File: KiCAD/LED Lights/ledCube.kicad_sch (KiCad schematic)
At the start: 14 parts, among them P1 CONN_01X03, P2 CONN_01X02, P3 CONN_01X02, P4 CONN_01X02, P5 CONN_01X02, U1 AL8805W5

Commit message: clean up
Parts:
- P1: value CONN_01X03 -> Power
- P2, P4: value CONN_01X02 -> LED +VE
- P3, P5: value CONN_01X02 -> LED -VE
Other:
- moved on the sheet: C1, C2, D1, D2, L1, P1, P2, P3, P4, P5, R1, R2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

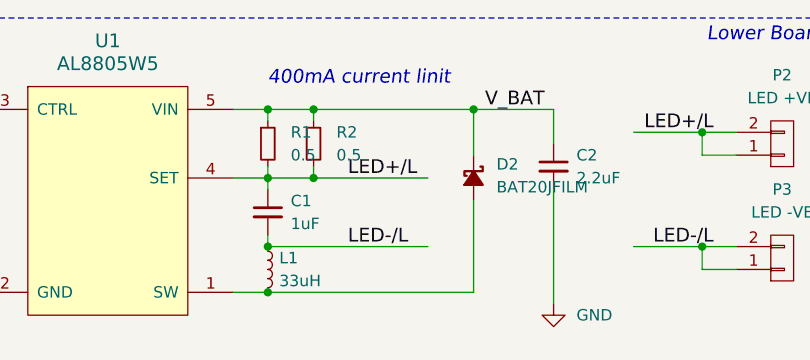
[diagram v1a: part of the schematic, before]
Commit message: 400 mA limit spelling fix
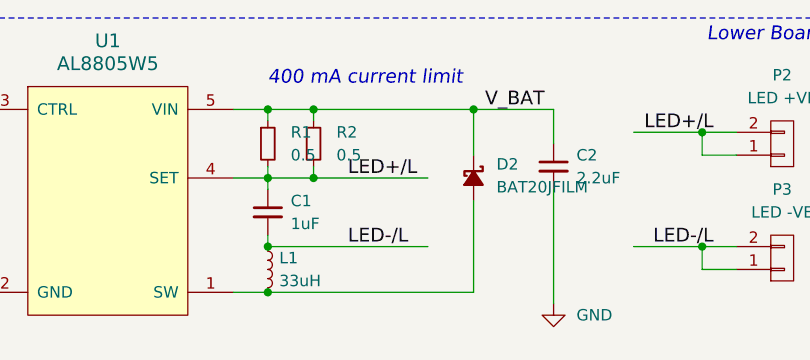
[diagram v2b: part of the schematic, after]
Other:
- note added: "400 mA current limit"
- note removed: "400mA current linit"
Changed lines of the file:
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@@
 		)
 	)
-	(text "400mA current linit"
+	(text "400 mA current limit"
 		(exclude_from_sim no)
 		(at 156.21 66.04 0)

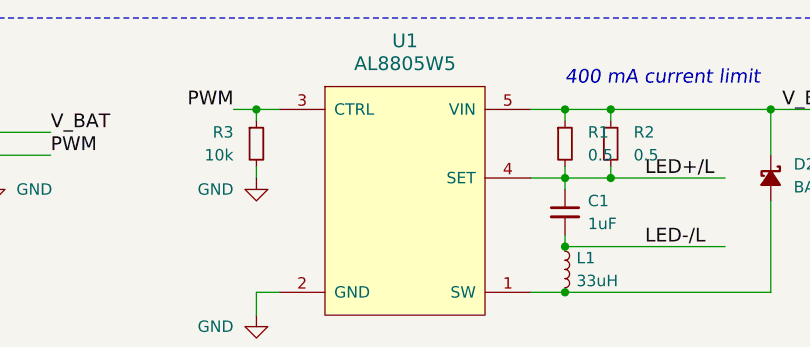
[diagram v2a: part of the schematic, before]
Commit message: Fixed Vendor spelling
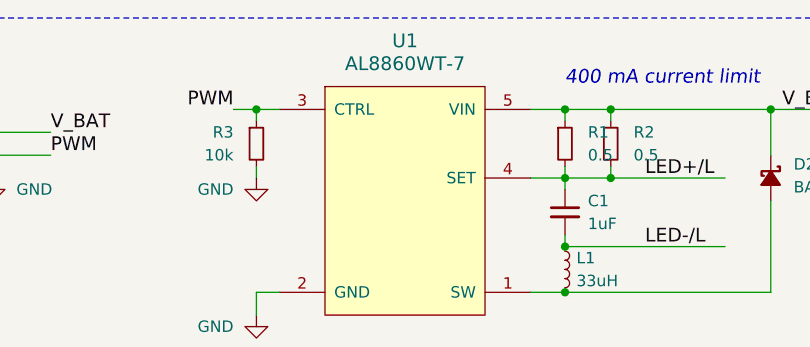
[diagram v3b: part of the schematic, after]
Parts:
- D1, D2, R1, R2: Vender DigiKey -> (none); Vendor (none) -> DigiKey
- L1: Vedner DigiKey -> (none); Vendor (none) -> DigiKey
- U1: value AL8805W5 -> AL8860WT-7; Part # AL8805W5-7DICT-ND -> AL8860WT-7DICT-ND; Vender DigiKey -> (none); Vendor (none) -> DigiKey
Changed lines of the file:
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@@
 			)
 		)
-		(property "Value" "AL8805W5"
+		(property "Value" "AL8860WT-7"
 			(at 138.43 63.5 0)
 			(effects
@@
 			)
 		)
-		(property "Datasheet" "https://cdn.sparkfun.com/datasheets/Components/LED/AL8805.pdf"
+		(property "Datasheet" "https://www.diodes.com/assets/Datasheets/AL8860.pdf"
 			(at 138.43 83.82 0)
 			(effects
@@
 			)
 		)
-		(property "Vender" "DigiKey"
+		(property "Vendor" "DigiKey"
 			(at 138.43 77.47 0)
 			(effects
@@
 			)
 		)
-		(property "Part #" "AL8805W5-7DICT-ND"
+		(property "Part #" "AL8860WT-7DICT-ND"
 			(at 138.43 77.47 0)
 			(effects
@@
 			)
 		)
-		(property "Datasheet" "~"
+		(property "Datasheet" "https://www.yageo.com/upload/media/product/app/datasheet/rchip/pyu-rl_group_521_rohs_l.pdf"
 			(at 156.21 72.39 0)
 			(effects
@@
 			)
 		)
-		(property "Vender" "DigiKey"
+		(property "Vendor" "DigiKey"
 			(at 156.21 72.39 90)
 			(effects
@@
 			)
 		)
-		(property "Vedner" "DigiKey"
+		(property "Vendor" "DigiKey"
 			(at 156.21 86.36 0)
 			(effects
@@
 			)
 		)
-		(property "Datasheet" "~"
+		(property "Datasheet" "https://www.yageo.com/upload/media/product/app/datasheet/rchip/pyu-rl_group_521_rohs_l.pdf"
 			(at 161.29 72.39 0)
 			(effects
@@
 			)
 		)
-		(property "Vender" "DigiKey"
+		(property "Vendor" "DigiKey"
 			(at 161.29 72.39 90)
 			(effects
@@
 			)
 		)
-		(property "Vender" "DigiKey"
+		(property "Vendor" "DigiKey"
 			(at 179.07 76.2 0)
 			(effects
@@
 			)
 		)
-		(property "Vender" "DigiKey"
+		(property "Vendor" "DigiKey"
 			(at 140.97 111.76 0)
 			(effects
@@
 			)
 		)
-		(property "Datasheet" ""
+		(property "Datasheet" "~"
 			(at 85.09 71.12 0)
 			(effects
@@
 			)
 		)
-		(property "Datasheet" ""
+		(property "Datasheet" "~"
 			(at 213.36 72.39 0)
 			(effects
@@
 			)
 		)
-		(property "Datasheet" ""
+		(property "Datasheet" "~"
 			(at 213.36 85.09 0)
 			(effects
@@
 			)
 		)
-		(property "Datasheet" ""
+		(property "Datasheet" "~"
 			(at 85.09 110.49 0)
 			(effects
@@
 			)
 		)
-		(property "Datasheet" ""
+		(property "Datasheet" "~"
 			(at 85.09 123.19 0)
 			(effects

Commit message: 3D model for the LED
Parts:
- D1: Farnell (none) -> 3430040
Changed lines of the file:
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@@
+			)
+		)
+		(property "Farnell" "3430040"
+			(at 140.97 111.76 0)
+			(effects
+				(font
+					(size 1.524 1.524)
+				)
+				(hide yes)
 			)
 		)
